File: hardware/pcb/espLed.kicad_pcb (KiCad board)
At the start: 2 copper layers, 30.5 x 35.6 mm, 23 parts, among them J1 led_strip, J2 flashing, J3 power, Q1 IRF9310TRPBF, Q2 AO3400A, Q3 AO3400A, Q4 AO3400A, SW1 reset, SW2 flash, U1 AMS1117-3.3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

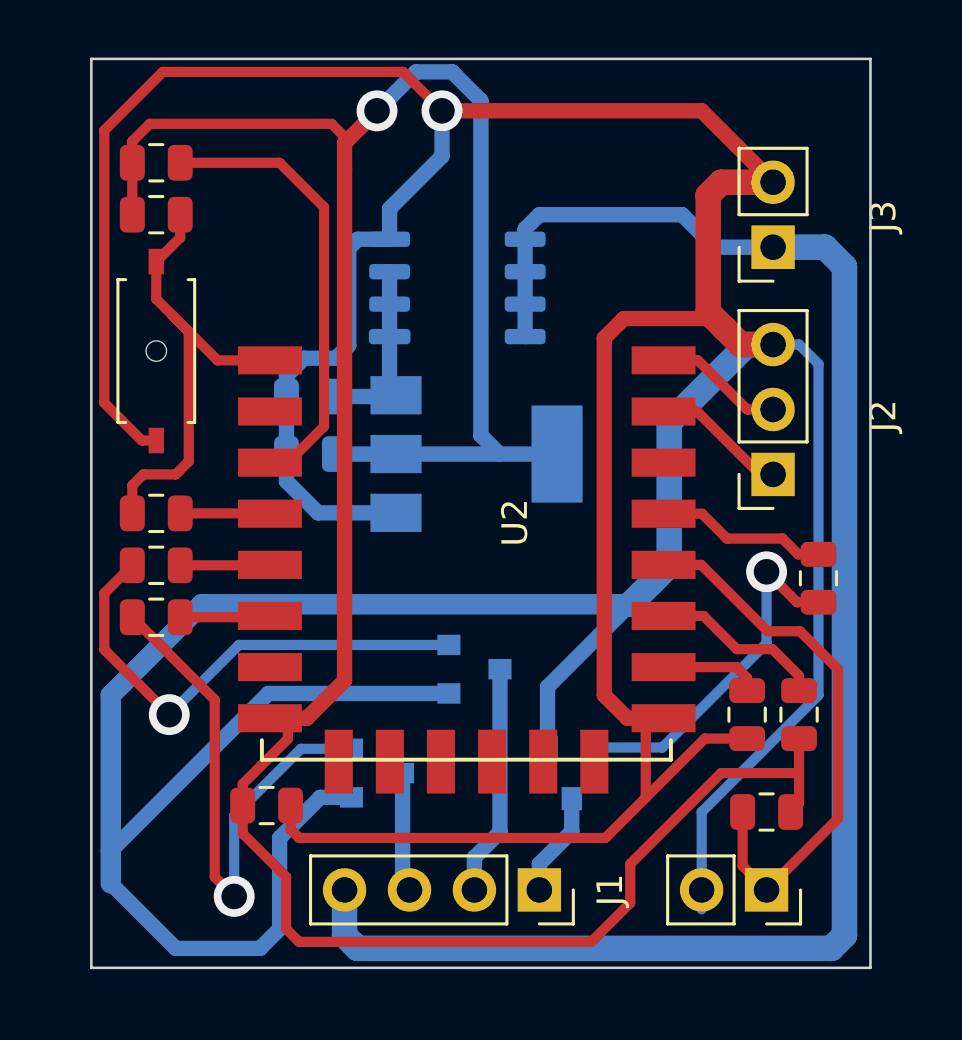
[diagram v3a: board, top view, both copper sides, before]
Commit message: move components on the left side downwards to save space
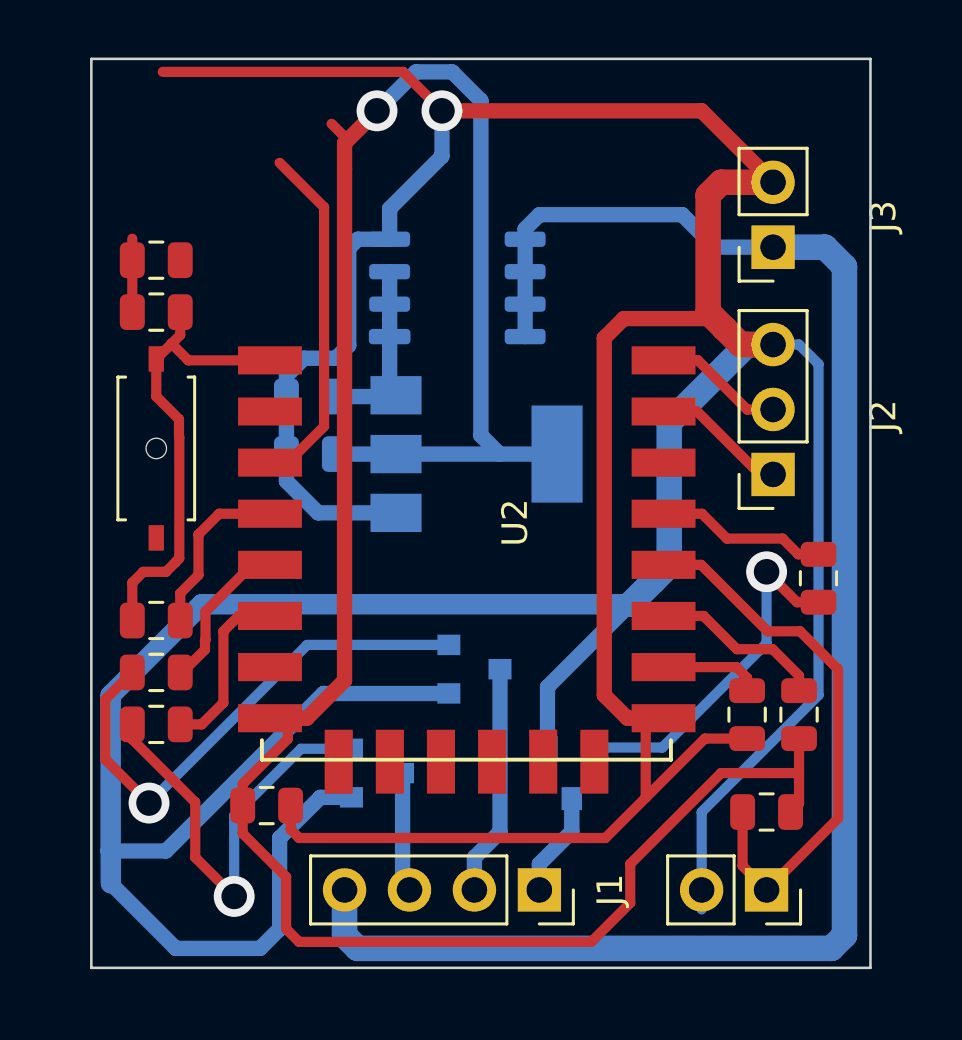
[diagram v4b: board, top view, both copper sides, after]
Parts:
- moved R1 4.19 mm to (167.1, 130.4)
- moved R2 4.19 mm to (167.1, 132.5)
- moved R5 4.19 mm to (167.1, 128.4)
- moved R6 3.81 mm to (167.1, 114.3)
- moved SW1 3.81 mm to (167.1, 121.7)
- moved R4 3.81 mm to (167.1, 116.3)
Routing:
- net GND: track 227.3 -> 210.7 mm
- net +3V3: track 103.8 -> 95.7 mm
- net Net-(Q4-Pad2): track 21.4 -> 17.2 mm
- net Net-(R6-Pad2): track 17.0 -> 13.1 mm
- net /led3: track 4.23 -> 7.67 mm
- net Net-(R5-Pad1): track 4.22 -> 7.51 mm
- net /led2: track 4.22 -> 6.84 mm
- net Net-(Q3-Pad2): track 19.4 -> 20.5 mm
- net Net-(R4-Pad2): track 20.0 -> 19.0 mm

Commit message: move power vias to the left and reconnect everything
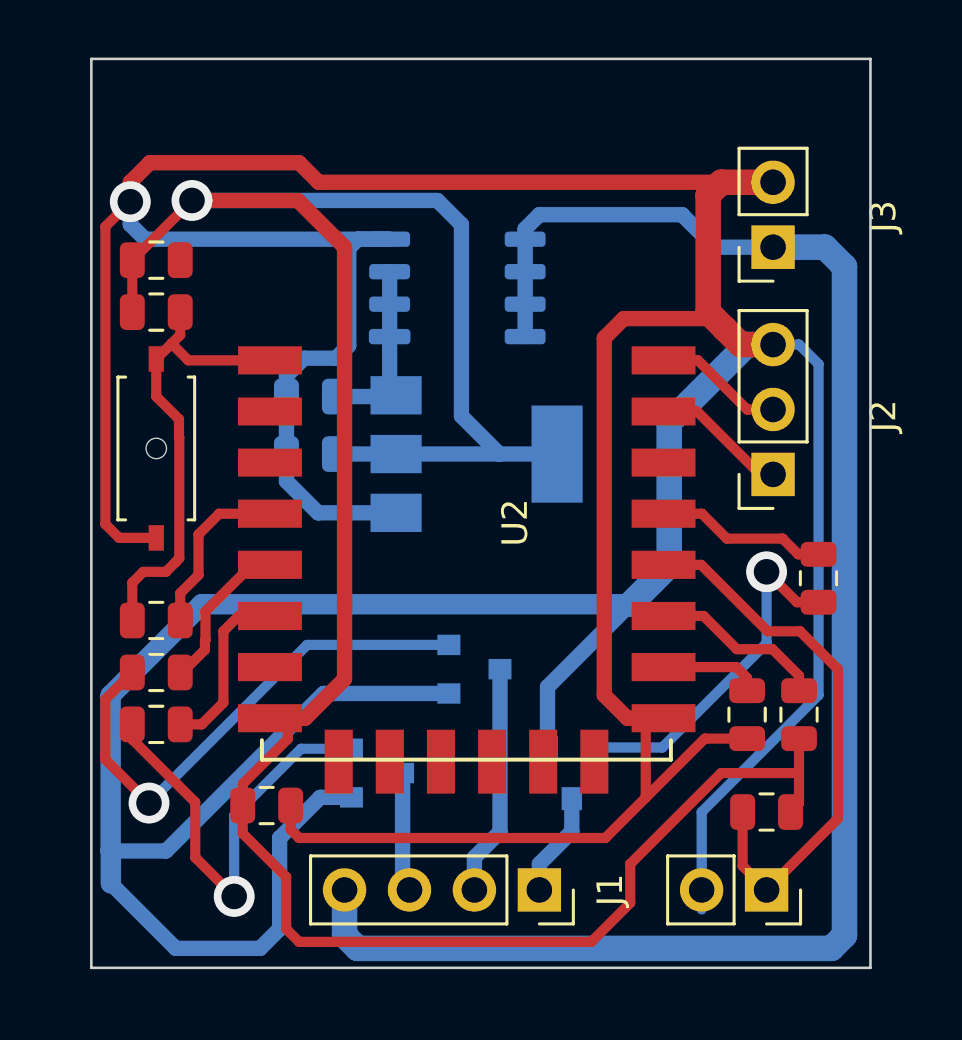
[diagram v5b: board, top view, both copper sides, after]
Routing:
- net GND: track 210.7 -> 232.2 mm
- net Net-(R6-Pad2): track 13.1 -> 0.07 mm
- net +3V3: track 95.7 -> 97.6 mm
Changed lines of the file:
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@@
     (thickness 1.6)
     (drawings 6)
-    (tracks 219)
+    (tracks 218)
     (zones 0)
     (modules 23)
@@
   (segment (start 189.357 116.967) (end 188.722 116.332) (width 1) (layer F.Cu) (net 1))
   (segment (start 189.992 117.602) (end 189.357 116.967) (width 1) (layer F.Cu) (net 1))
-  (via (at 178.308 108.458) (size 1.6) (drill 1) (layers F.Cu B.Cu) (net 1))
-  (segment (start 191.262 111.252) (end 188.468 108.458) (width 0.6) (layer F.Cu) (net 1))
-  (segment (start 188.468 108.458) (end 178.308 108.458) (width 0.6) (layer F.Cu) (net 1))
-  (segment (start 176.784 106.934) (end 167.386 106.934) (width 0.4) (layer F.Cu) (net 1))
-  (segment (start 178.308 108.458) (end 176.784 106.934) (width 0.4) (layer F.Cu) (net 1))
   (segment (start 176.462 123.7) (end 176.512 123.65) (width 0.4) (layer B.Cu) (net 1))
   (segment (start 172.2245 121.886) (end 172.2245 119.636) (width 0.6) (layer B.Cu) (net 1))
-  (segment (start 178.308 110.236) (end 178.308 108.458) (width 0.6) (layer B.Cu) (net 1))
-  (segment (start 176.262 112.282) (end 178.308 110.236) (width 0.6) (layer B.Cu) (net 1))
-  (segment (start 176.262 113.481) (end 176.262 112.282) (width 0.6) (layer B.Cu) (net 1))
   (segment (start 172.2245 118.8235) (end 172.912 118.136) (width 0.6) (layer B.Cu) (net 1))
   (segment (start 172.2245 119.636) (end 172.2245 118.8235) (width 0.6) (layer B.Cu) (net 1))
@@
   (segment (start 165.354 137.414) (end 165.347752 137.407752) (width 0.8) (layer B.Cu) (net 1))
   (segment (start 165.347752 137.407752) (end 165.347752 131.324248) (width 0.8) (layer B.Cu) (net 1))
+  (via (at 166.116 112.014) (size 1.6) (drill 1) (layers F.Cu B.Cu) (net 1))
+  (segment (start 166.116 112.903) (end 166.116 112.014) (width 0.6) (layer B.Cu) (net 1))
+  (segment (start 166.694 113.481) (end 166.116 112.903) (width 0.6) (layer B.Cu) (net 1))
+  (segment (start 176.262 113.481) (end 166.694 113.481) (width 0.6) (layer B.Cu) (net 1))
+  (segment (start 166.116 111.252) (end 166.116 112.014) (width 0.6) (layer F.Cu) (net 1))
+  (segment (start 166.878 110.49) (end 166.116 111.252) (width 0.6) (layer F.Cu) (net 1))
+  (segment (start 172.72 110.49) (end 166.878 110.49) (width 0.6) (layer F.Cu) (net 1))
+  (segment (start 173.482 111.252) (end 172.72 110.49) (width 0.6) (layer F.Cu) (net 1))
+  (segment (start 191.262 111.252) (end 173.482 111.252) (width 0.6) (layer F.Cu) (net 1))
+  (segment (start 165.14201 112.98799) (end 166.116 112.014) (width 0.4) (layer F.Cu) (net 1))
+  (segment (start 165.14201 124.62901) (end 165.14201 112.98799) (width 0.4) (layer F.Cu) (net 1))
+  (segment (start 165.679 125.166) (end 165.14201 124.62901) (width 0.4) (layer F.Cu) (net 1))
+  (segment (start 167.132 125.166) (end 165.679 125.166) (width 0.4) (layer F.Cu) (net 1))
   (segment (start 174.0995 119.636) (end 176.462 119.636) (width 0.6) (layer B.Cu) (net 2))
   (segment (start 176.262 117.291) (end 176.262 114.751) (width 0.6) (layer B.Cu) (net 2))
@@
   (segment (start 192.278 133.0175) (end 192.278 134.366) (width 0.4) (layer F.Cu) (net 3))
   (segment (start 192.278 134.366) (end 192.278 135.5575) (width 0.4) (layer F.Cu) (net 3))
-  (segment (start 166.1945 114.3) (end 166.1945 113.7135) (width 0.4) (layer F.Cu) (net 3))
-  (segment (start 173.99 108.966) (end 174.498 109.474) (width 0.4) (layer F.Cu) (net 3))
-  (segment (start 166.1945 114.3) (end 166.1945 113.4595) (width 0.4) (layer F.Cu) (net 3))
-  (segment (start 179.832 108.057998) (end 178.708002 106.934) (width 0.6) (layer B.Cu) (net 3))
-  (via (at 175.768 108.458) (size 1.6) (drill 1) (layers F.Cu B.Cu) (net 3))
-  (segment (start 177.292 106.934) (end 175.768 108.458) (width 0.6) (layer B.Cu) (net 3))
-  (segment (start 178.708002 106.934) (end 177.292 106.934) (width 0.6) (layer B.Cu) (net 3))
-  (segment (start 174.498 109.728) (end 174.498 110.744) (width 0.6) (layer F.Cu) (net 3))
-  (segment (start 175.768 108.458) (end 174.498 109.728) (width 0.6) (layer F.Cu) (net 3))
-  (segment (start 174.498 109.474) (end 174.498 110.744) (width 0.4) (layer F.Cu) (net 3))
-  (segment (start 179.832 121.158) (end 180.56 121.886) (width 0.6) (layer B.Cu) (net 3))
-  (segment (start 179.832 108.057998) (end 179.832 121.158) (width 0.6) (layer B.Cu) (net 3))
   (segment (start 180.56 121.886) (end 182.812 121.886) (width 0.6) (layer B.Cu) (net 3))
   (segment (start 176.512 121.886) (end 180.56 121.886) (width 0.6) (layer B.Cu) (net 3))
-  (segment (start 173.0245 132.22) (end 172.28 132.22) (width 0.6) (layer F.Cu) (net 3))
-  (segment (start 174.498 130.7465) (end 173.0245 132.22) (width 0.6) (layer F.Cu) (net 3))
-  (segment (start 174.498 110.744) (end 174.498 130.7465) (width 0.6) (layer F.Cu) (net 3))
   (segment (start 172.28 133.028) (end 172.28 132.22) (width 0.4) (layer F.Cu) (net 3))
   (segment (start 170.5125 134.7955) (end 172.28 133.028) (width 0.4) (layer F.Cu) (net 3))
@@
   (segment (start 189.23 134.366) (end 185.674 137.922) (width 0.4) (layer F.Cu) (net 3))
   (segment (start 192.278 134.366) (end 189.23 134.366) (width 0.4) (layer F.Cu) (net 3))
+  (via (at 168.529002 111.965484) (size 1.6) (drill 1) (layers F.Cu B.Cu) (net 3))
+  (segment (start 179.07 120.396) (end 179.07 112.903) (width 0.6) (layer B.Cu) (net 3))
+  (segment (start 179.07 112.903) (end 178.132484 111.965484) (width 0.6) (layer B.Cu) (net 3))
+  (segment (start 168.529002 111.965498) (end 168.529002 111.965484) (width 0.4) (layer F.Cu) (net 3))
+  (segment (start 178.132484 111.965484) (end 168.529002 111.965484) (width 0.6) (layer B.Cu) (net 3))
+  (segment (start 166.1945 114.3) (end 168.529002 111.965498) (width 0.4) (layer F.Cu) (net 3))
+  (segment (start 180.56 121.886) (end 179.07 120.396) (width 0.6) (layer B.Cu) (net 3))
+  (segment (start 174.498 113.792) (end 172.671484 111.965484) (width 0.6) (layer F.Cu) (net 3))
+  (segment (start 174.498 130.683) (end 174.498 113.792) (width 0.6) (layer F.Cu) (net 3))
+  (segment (start 172.671484 111.965484) (end 168.529002 111.965484) (width 0.6) (layer F.Cu) (net 3))
+  (segment (start 172.961 132.22) (end 174.498 130.683) (width 0.6) (layer F.Cu) (net 3))
+  (segment (start 172.28 132.22) (end 172.961 132.22) (width 0.6) (layer F.Cu) (net 3))
   (segment (start 176.768 138.668) (end 177.038 138.938) (width 0.6) (layer B.Cu) (net 4))
   (segment (start 176.768 134.366) (end 176.768 138.668) (width 0.6) (layer B.Cu) (net 4))
@@
   (segment (start 168.0695 128.397) (end 168.0695 127.3325) (width 0.4) (layer F.Cu) (net 17))
   (segment (start 172.234 122.174) (end 172.28 122.22) (width 0.4) (layer F.Cu) (net 18))
-  (segment (start 173.697989 112.229989) (end 171.958 110.49) (width 0.4) (layer F.Cu) (net 18))
-  (segment (start 173.697989 120.802011) (end 173.697989 112.229989) (width 0.4) (layer F.Cu) (net 18))
-  (segment (start 172.28 122.22) (end 173.697989 120.802011) (width 0.4) (layer F.Cu) (net 18))
   (segment (start 186.28 126.22) (end 186.298 126.238) (width 0.4) (layer F.Cu) (net 19))
   (segment (start 186.4375 126.0625) (end 186.28 126.22) (width 0.4) (layer F.Cu) (net 19))

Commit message: connect forgotten wire and fix board outline
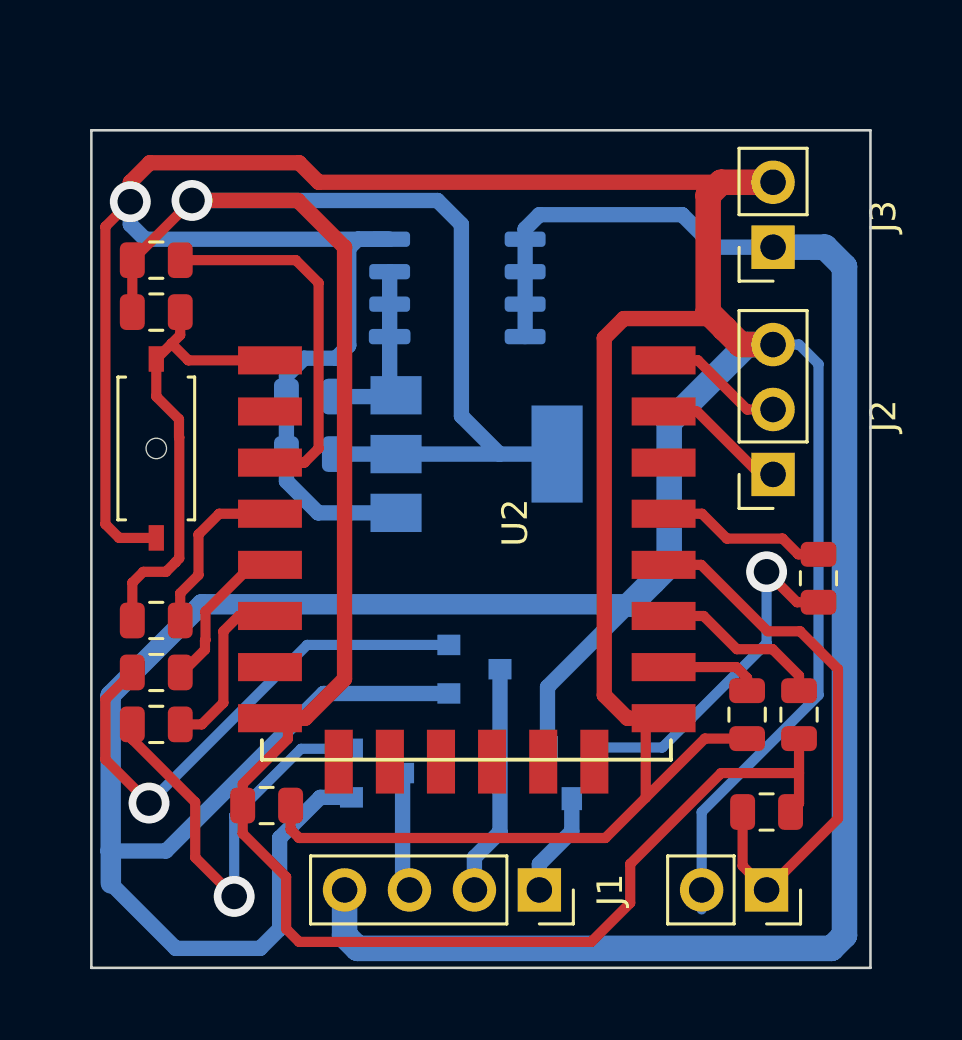
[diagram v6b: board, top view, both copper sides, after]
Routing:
- net Net-(R6-Pad2): track 0.07 -> 13.8 mm
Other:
- board size 30.5 x 35.6 mm -> 30.5 x 32.8 mm
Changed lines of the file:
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@@
     (thickness 1.6)
     (drawings 6)
-    (tracks 218)
+    (tracks 223)
     (zones 0)
     (modules 23)
@@
   )
   (dimension 30.48 (width 0.15) (layer Dwgs.User)
-    (gr_text "30,480 mm" (at 179.832 103.348) (layer Dwgs.User)
-      (effects (font (size 1 1) (thickness 0.15)))
-    )
-    (feature1 (pts (xy 195.072 106.426) (xy 195.072 104.061579)))
-    (feature2 (pts (xy 164.592 106.426) (xy 164.592 104.061579)))
-    (crossbar (pts (xy 164.592 104.648) (xy 195.072 104.648)))
-    (arrow1a (pts (xy 195.072 104.648) (xy 193.945496 105.234421)))
-    (arrow1b (pts (xy 195.072 104.648) (xy 193.945496 104.061579)))
-    (arrow2a (pts (xy 164.592 104.648) (xy 165.718504 105.234421)))
-    (arrow2b (pts (xy 164.592 104.648) (xy 165.718504 104.061579)))
-  )
-  (dimension 35.56 (width 0.15) (layer Dwgs.User)
-    (gr_text "35,560 mm" (at 198.15 124.206 270) (layer Dwgs.User)
-      (effects (font (size 1 1) (thickness 0.15)))
-    )
-    (feature1 (pts (xy 195.072 141.986) (xy 197.436421 141.986)))
-    (feature2 (pts (xy 195.072 106.426) (xy 197.436421 106.426)))
-    (crossbar (pts (xy 196.85 106.426) (xy 196.85 141.986)))
-    (arrow1a (pts (xy 196.85 141.986) (xy 196.263579 140.859496)))
-    (arrow1b (pts (xy 196.85 141.986) (xy 197.436421 140.859496)))
-    (arrow2a (pts (xy 196.85 106.426) (xy 196.263579 107.552504)))
-    (arrow2b (pts (xy 196.85 106.426) (xy 197.436421 107.552504)))
-  )
-  (gr_line (start 195.072 106.426) (end 195.072 141.986) (layer Edge.Cuts) (width 0.1))
-  (gr_line (start 164.592 106.426) (end 195.072 106.426) (layer Edge.Cuts) (width 0.1))
-  (gr_line (start 164.592 141.986) (end 164.592 106.426) (layer Edge.Cuts) (width 0.1))
+    (gr_text "30.480 мм" (at 179.832 106.269) (layer Dwgs.User)
+      (effects (font (size 1 1) (thickness 0.15)))
+    )
+    (feature1 (pts (xy 195.072 109.22) (xy 195.072 106.982579)))
+    (feature2 (pts (xy 164.592 109.22) (xy 164.592 106.982579)))
+    (crossbar (pts (xy 164.592 107.569) (xy 195.072 107.569)))
+    (arrow1a (pts (xy 195.072 107.569) (xy 193.945496 108.155421)))
+    (arrow1b (pts (xy 195.072 107.569) (xy 193.945496 106.982579)))
+    (arrow2a (pts (xy 164.592 107.569) (xy 165.718504 108.155421)))
+    (arrow2b (pts (xy 164.592 107.569) (xy 165.718504 106.982579)))
+  )
+  (dimension 32.766 (width 0.15) (layer Dwgs.User)
+    (gr_text "32.766 мм" (at 198.277 125.603 90) (layer Dwgs.User)
+      (effects (font (size 1 1) (thickness 0.15)))
+    )
+    (feature1 (pts (xy 195.072 109.22) (xy 197.563421 109.22)))
+    (feature2 (pts (xy 195.072 141.986) (xy 197.563421 141.986)))
+    (crossbar (pts (xy 196.977 141.986) (xy 196.977 109.22)))
+    (arrow1a (pts (xy 196.977 109.22) (xy 197.563421 110.346504)))
+    (arrow1b (pts (xy 196.977 109.22) (xy 196.390579 110.346504)))
+    (arrow2a (pts (xy 196.977 141.986) (xy 197.563421 140.859496)))
+    (arrow2b (pts (xy 196.977 141.986) (xy 196.390579 140.859496)))
+  )
+  (gr_line (start 195.072 109.22) (end 195.072 141.986) (layer Edge.Cuts) (width 0.1))
+  (gr_line (start 164.592 109.22) (end 195.072 109.22) (layer Edge.Cuts) (width 0.1))
+  (gr_line (start 164.592 141.986) (end 164.592 109.22) (layer Edge.Cuts) (width 0.1))
   (gr_line (start 195.072 141.986) (end 164.592 141.986) (layer Edge.Cuts) (width 0.1))
   (segment (start 172.2245 122.9485) (end 172.2245 121.886) (width 0.6) (layer B.Cu) (net 1))
@@
   (segment (start 168.0695 128.397) (end 168.0695 127.3325) (width 0.4) (layer F.Cu) (net 17))
   (segment (start 172.234 122.174) (end 172.28 122.22) (width 0.4) (layer F.Cu) (net 18))
+  (segment (start 172.593 114.3) (end 168.0695 114.3) (width 0.4) (layer F.Cu) (net 18))
+  (segment (start 173.482 121.666) (end 173.482 115.189) (width 0.4) (layer F.Cu) (net 18))
+  (segment (start 172.928 122.22) (end 173.482 121.666) (width 0.4) (layer F.Cu) (net 18))
+  (segment (start 173.482 115.189) (end 172.593 114.3) (width 0.4) (layer F.Cu) (net 18))
+  (segment (start 172.28 122.22) (end 172.928 122.22) (width 0.4) (layer F.Cu) (net 18))
   (segment (start 186.28 126.22) (end 186.298 126.238) (width 0.4) (layer F.Cu) (net 19))
   (segment (start 186.4375 126.0625) (end 186.28 126.22) (width 0.4) (layer F.Cu) (net 19))
